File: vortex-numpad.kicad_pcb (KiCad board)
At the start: 2 copper layers, 76.2 x 117.5 mm, 60 parts, among them J1 USB_B_Micro, SW1 SW_Push, U1 ATmega32U4-AU, Y1 16MHz

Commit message: Most switch tracks in place, terrible
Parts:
- moved C3 1.77 mm to (117.5, 77.8), turned to 0 degrees
- moved D11 1.59 mm to (123.8, 115.9)
- moved D18 1.59 mm to (123.8, 154.0)
- moved C1 0.79 mm to (123.8, 86.5)
- moved C2 0.79 mm to (123.8, 83.3)
- moved C4 0.79 mm to (87.3, 86.5)
- moved C5 0.79 mm to (92.1, 84.9)
- moved C7 0.79 mm to (87.3, 83.3)
- moved FN1 0.79 mm to (77.8, 73.0)
- moved FN2 0.79 mm to (96.8, 73.0)
- moved FN3 0.79 mm to (115.9, 73.0)
- moved FN4 0.79 mm to (134.9, 73.0)
- moved J1 0.79 mm to (87.3, 66.2)
- moved Y1 0.79 mm to (117.5, 85.1)
- moved C6 0.79 mm to (88.9, 77.8), turned to 90 degrees
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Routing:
- net ROW1: track 0.00 -> 62.9 mm
- net ROW5: track 0.00 -> 49.4 mm
- net ROW3: track 0.00 -> 49.4 mm
- net ROW4: track 0.00 -> 41.7 mm
- net ROW2: track 0.00 -> 41.0 mm
- net ROW0: track 0.00 -> 21.6 mm
- net Net-(D2-Pad2): track 0.00 -> 11.1 mm
- net Net-(D18-Pad2): track 0.00 -> 8.12 mm
- net Net-(D11-Pad2): track 0.00 -> 8.03 mm
- net Net-(D1-Pad2): track 0.00 -> 7.89 mm
- net Net-(D15-Pad2): track 0.00 -> 7.30 mm
- net Net-(D17-Pad2): track 0.00 -> 6.62 mm
- net Net-(D16-Pad2): track 0.00 -> 6.62 mm
- net Net-(D8-Pad2): track 0.00 -> 6.62 mm
- net Net-(D6-Pad2): track 0.00 -> 6.62 mm
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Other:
- board size 76.2 x 117.5 mm -> 76.2 x 116.7 mm
- net class Default: trace_width 0.25 -> 0.254
- net class Power added: clearance 0.2, trace_width 0.381, via_dia 0.8, via_drill 0.4

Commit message: Initial traces all done
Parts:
- C1, C2: value 1uF -> 22uF
- D2: moved to F.Cu
- moved R4 60.1 mm to (134.0, 85.8)
- moved R1 54.3 mm to (128.4, 79.8), turned to 0 degrees
- moved C5 32.5 mm to (123.8, 78.2), turned to 90 degrees
- moved C2 25.8 mm to (104.1, 66.7), turned to 270 degrees
- moved C1 24.5 mm to (109.5, 66.7), turned to 270 degrees
- moved C4 22.0 mm to (107.8, 94.5), turned to 90 degrees
- moved C3 20.7 mm to (96.8, 78.7), turned to 270 degrees
- moved R3 19.8 mm to (93.7, 85.1)
- moved R2 19.3 mm to (93.7, 82.4)
- moved C7 18.8 mm to (104.8, 90.3)
- moved Y1 17.6 mm to (106.4, 71.4), turned to 180 degrees
- moved C6 16.7 mm to (99.7, 65.0), turned to 0 degrees
- moved D2 1.46 mm to (93.7, 79.2)
- moved F1 1.40 mm to (84.3, 77.7)
- turned U1 to 0 degrees
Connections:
- C1 pad 1: Net-(C1-Pad1) -> GND
- C2 pad 2: Net-(C1-Pad1) -> Net-(C2-Pad2)
- U1 pad 16: Net-(C1-Pad1) -> Net-(C2-Pad2)
- Y1 pad 3: Net-(C1-Pad1) -> Net-(C2-Pad2)
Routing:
- net COL0: track 0.00 -> 154.1 mm, vias 0 -> 3
- net +5V: track 0.00 -> 152.1 mm, vias 0 -> 7
- net COL3: track 0.00 -> 143.4 mm, vias 0 -> 3
- net GND: track 0.00 -> 137.1 mm
- net COL1: track 0.00 -> 136.0 mm, vias 0 -> 3
- net ROW5: track 49.4 -> 178.2 mm, vias 0 -> 4
- net COL2: track 0.00 -> 116.8 mm, vias 0 -> 3
- net ROW4: track 41.7 -> 152.3 mm, vias 0 -> 4
- net ROW0: track 21.6 -> 128.4 mm, vias 0 -> 5
- net ROW3: track 49.4 -> 131.4 mm, vias 0 -> 4
- net ROW2: track 41.0 -> 105.4 mm, vias 0 -> 4
- net Net-(R1-Pad2): track 0.00 -> 36.1 mm, vias 0 -> 4
- net Net-(R4-Pad2): track 0.00 -> 22.6 mm
- net D-: track 0.00 -> 20.0 mm
- net ROW1: track 62.9 -> 82.8 mm, vias 0 -> 2
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
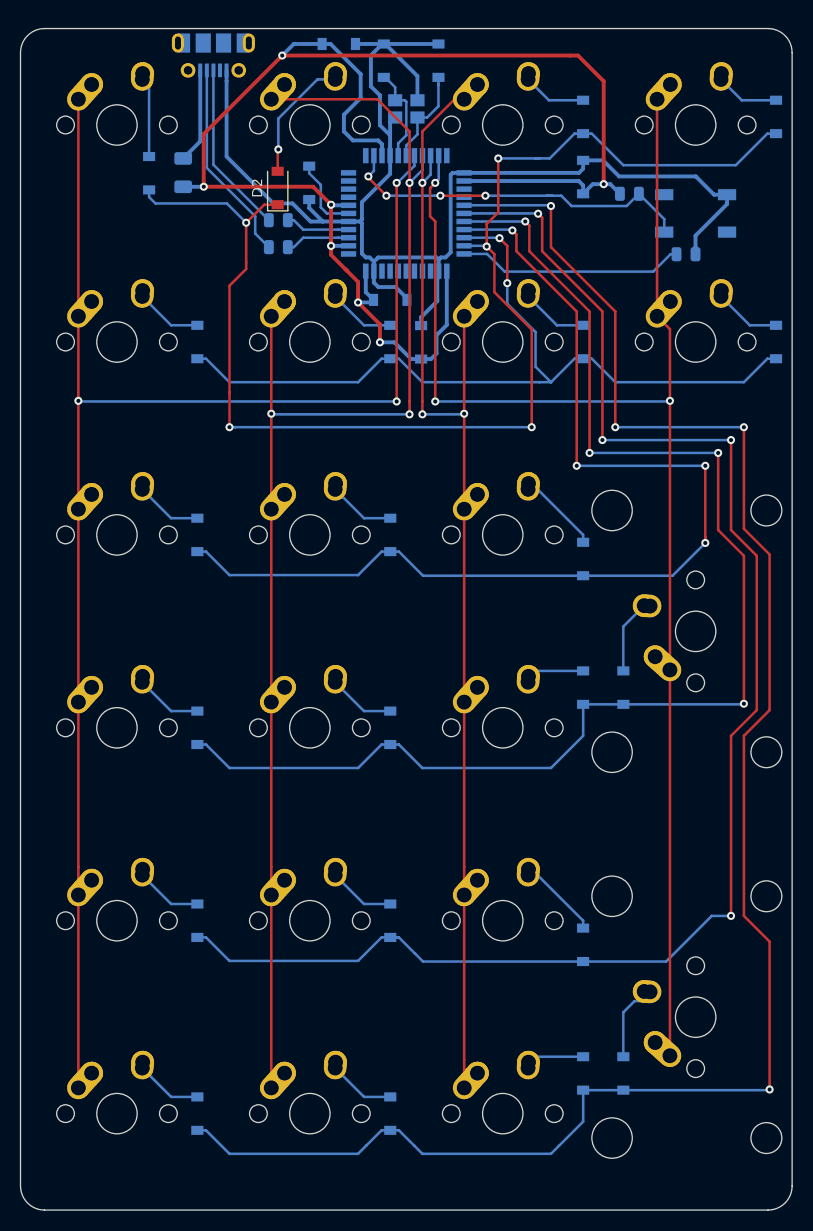
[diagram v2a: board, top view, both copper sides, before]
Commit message: Fixed mounting holes and associated spacing
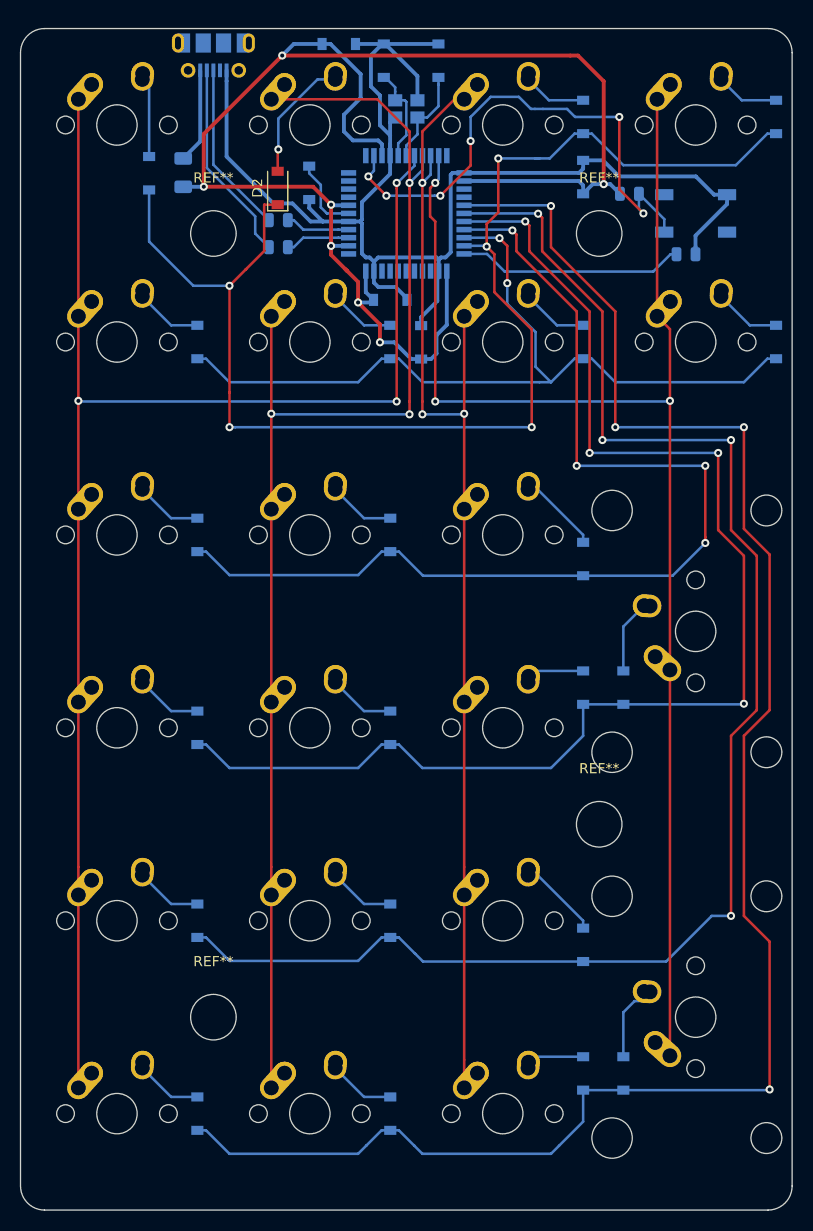
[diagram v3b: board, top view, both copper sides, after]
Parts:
- added REF**: MountingHole_4.5mm, MountingHole:MountingHole_4.5mm, F.Cu at (87.3, 161.1)
- added REF**: MountingHole_4.5mm, MountingHole:MountingHole_4.5mm, F.Cu at (125.4, 142.1)
- added REF**: MountingHole_4.5mm, MountingHole:MountingHole_4.5mm, F.Cu at (125.4, 83.7)
- added REF**: MountingHole_4.5mm, MountingHole:MountingHole_4.5mm, F.Cu at (87.3, 83.7)
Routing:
- net Net-(R1-Pad2): track 36.1 -> 53.0 mm, vias 4 -> 6
- net ROW0: track 128.4 -> 132.0 mm
